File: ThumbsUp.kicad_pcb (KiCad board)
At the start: 2 copper layers, 215.3 x 223 mm, 51 parts, among them J1 52559-1233, J10 Raiser_Male, J13 Raiser_Female, J14 Raiser_Male, J19 Raiser_Female, J1L1 PJ-3200B, J1R1 PJ-3200B, J2 52559-1233, J33 Raiser_Male, J34 Raiser_Female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

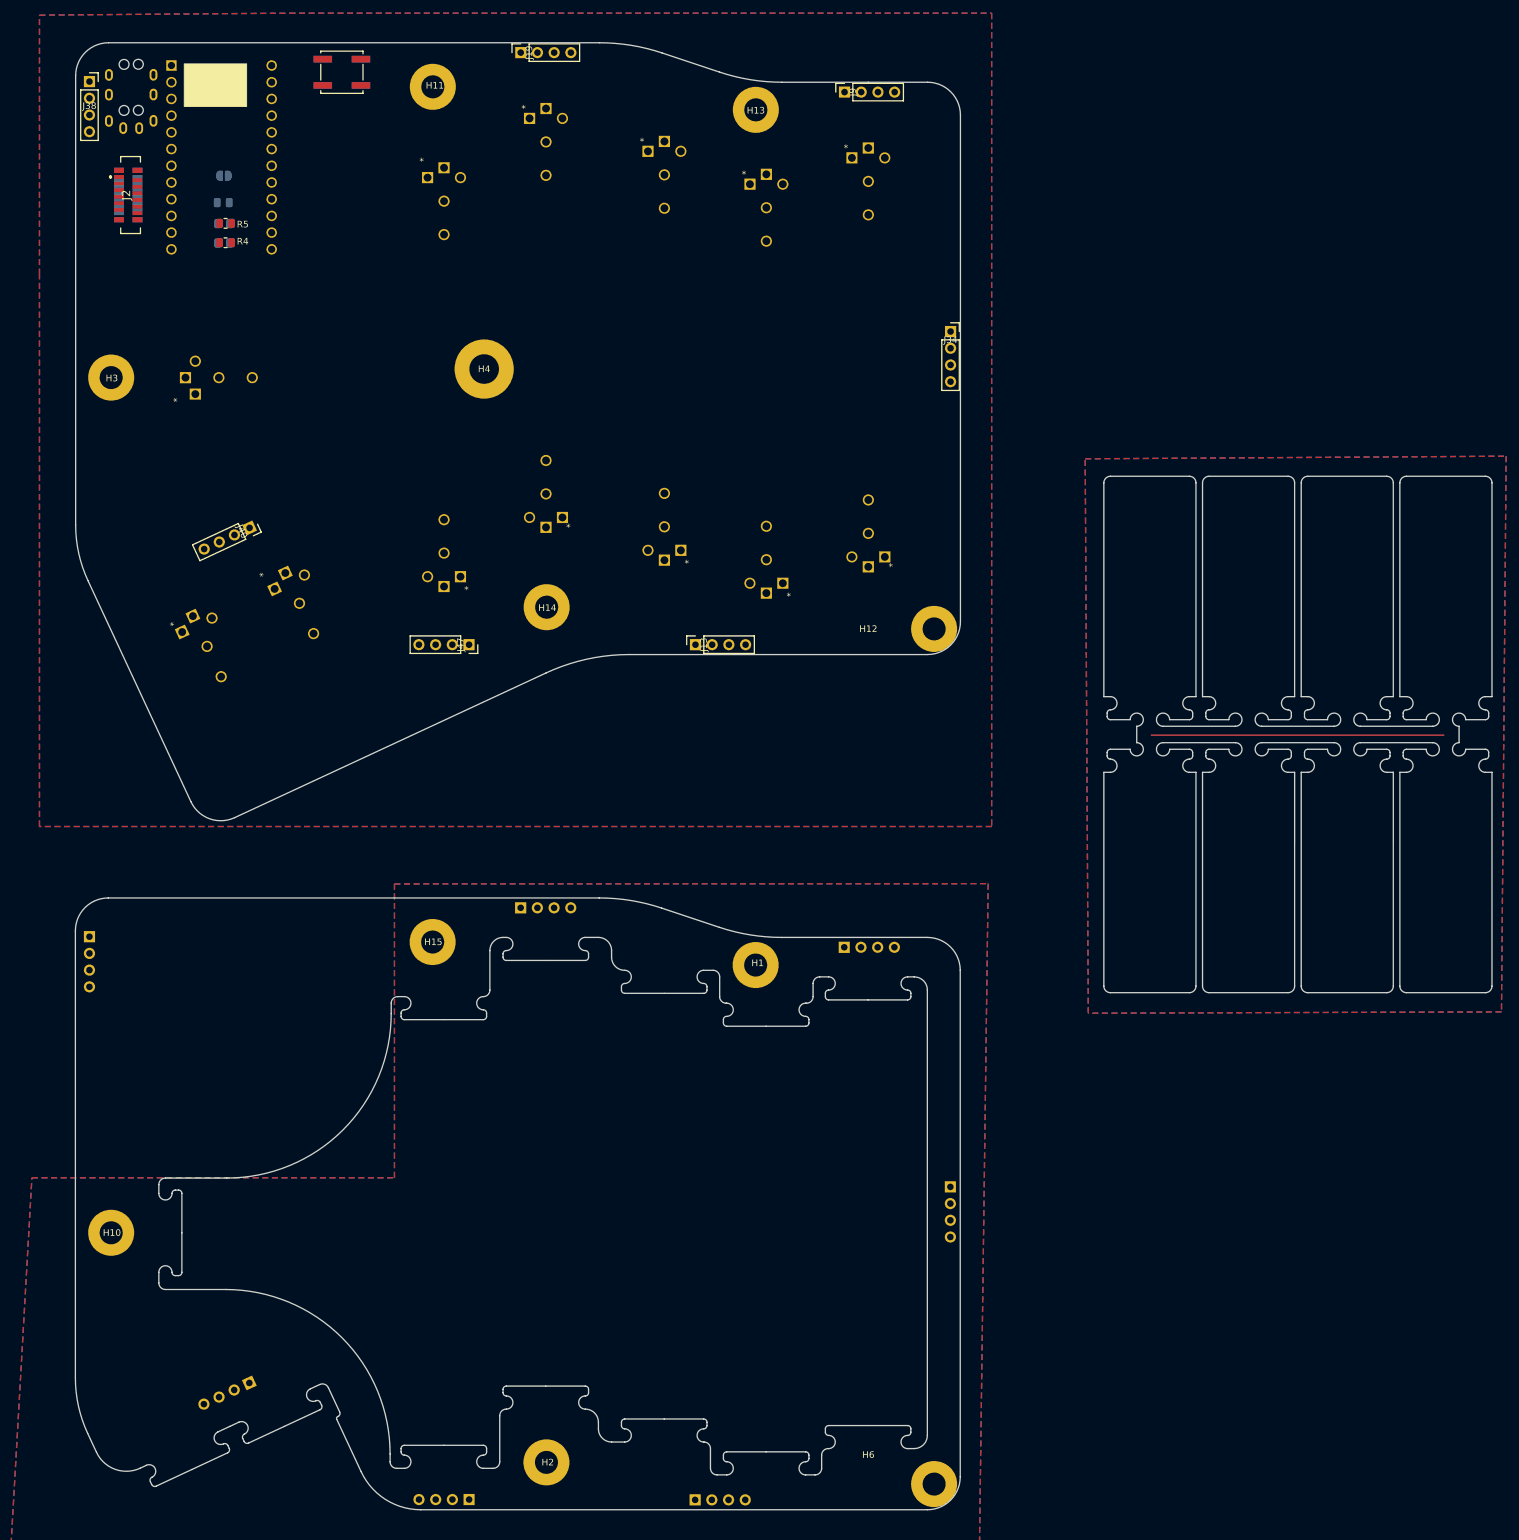
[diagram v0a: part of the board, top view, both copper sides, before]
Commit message: K12: Placed the tracks, text, etc. TODO: generate Gerbers.
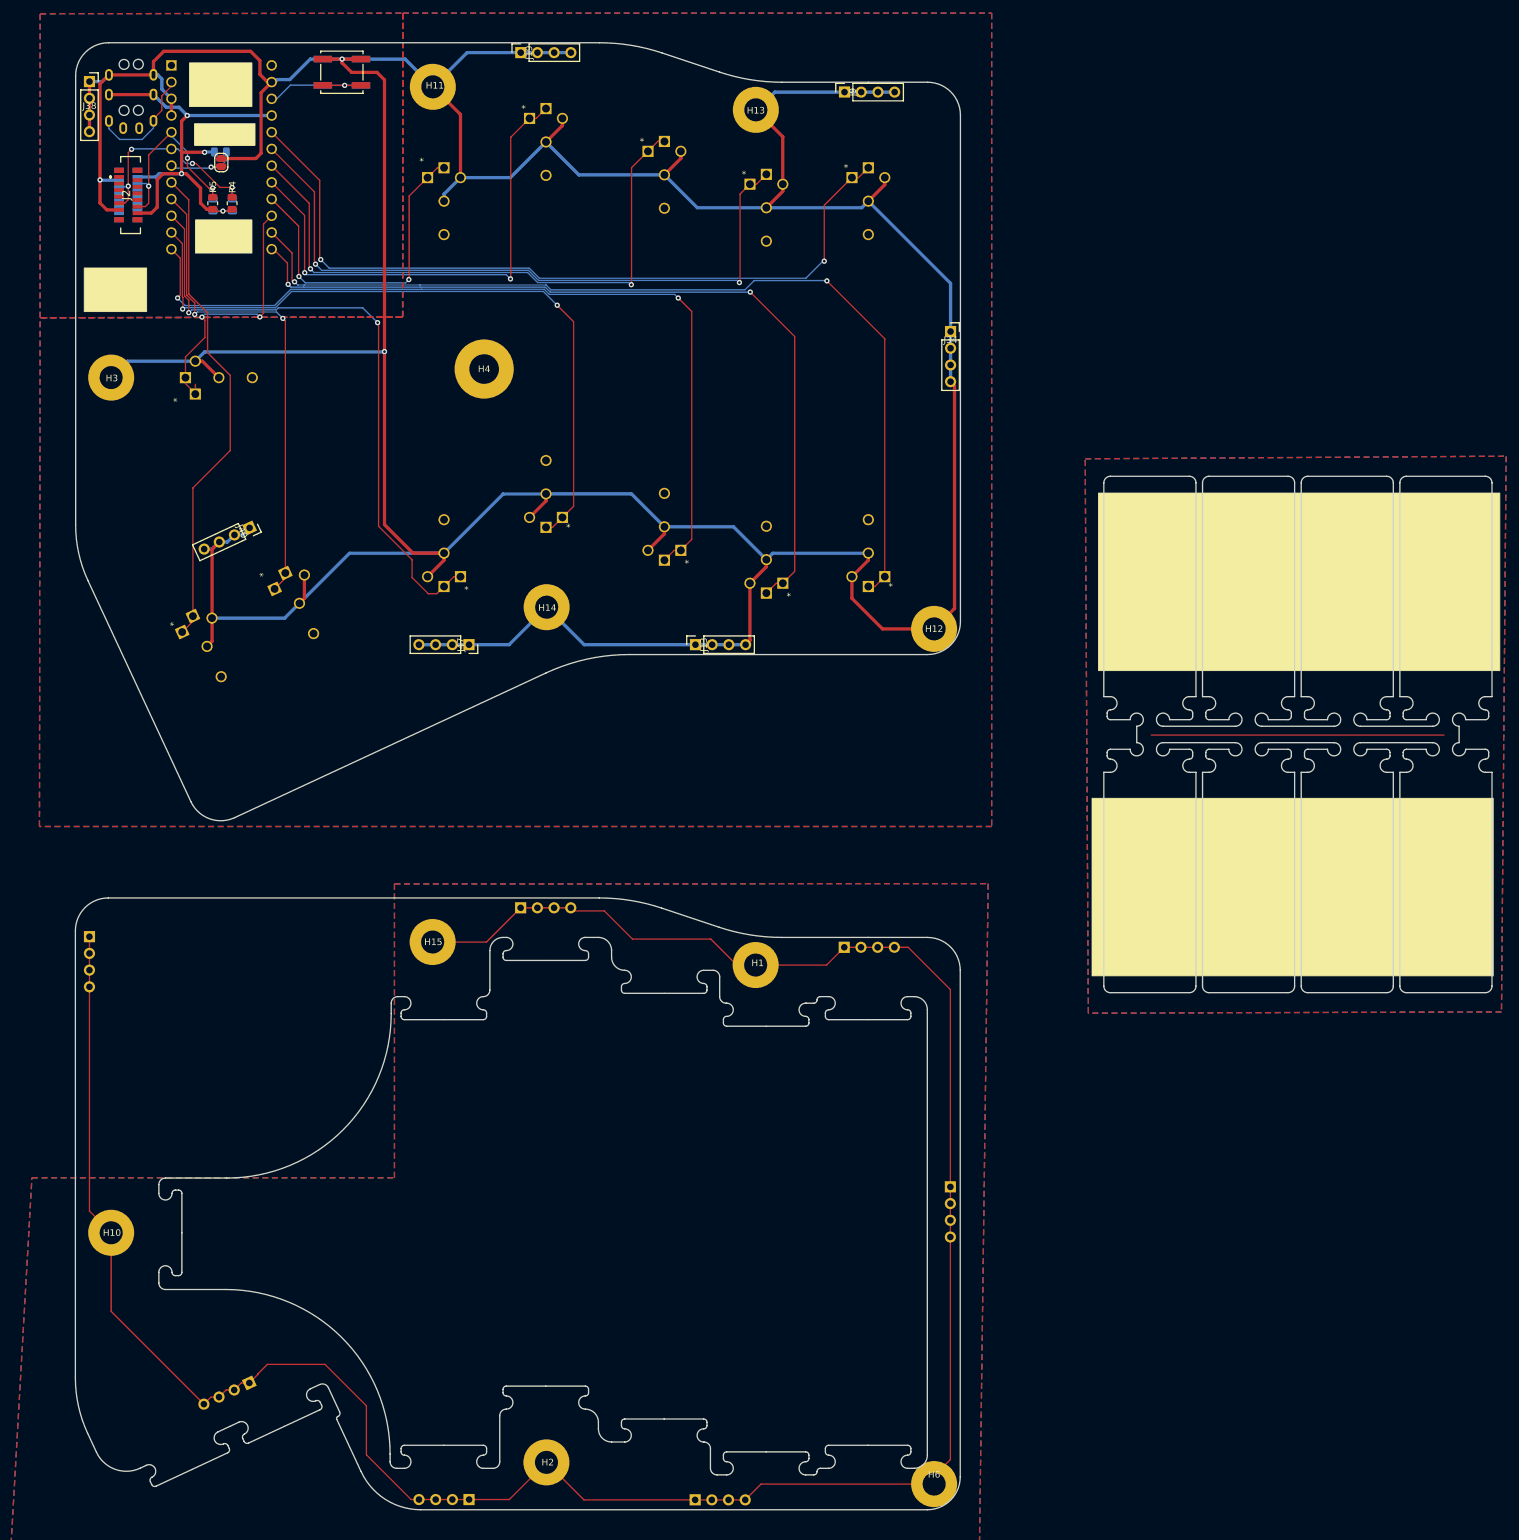
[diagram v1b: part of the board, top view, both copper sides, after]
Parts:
- JP1: moved to F.Cu
- moved H12 10.0 mm to (162.0, 114.6)
- moved H6 10.0 mm to (162.0, 244.6)
- moved R17 7.71 mm to (53.5, 42.1)
- moved R4 6.08 mm to (55.3, 49.9), turned to 90 degrees
- moved R2 5.93 mm to (55.3, 50.2), turned to 90 degrees
- moved R5 3.62 mm to (52.3, 49.9), turned to -90 degrees
- moved R1 3.26 mm to (52.4, 50.2), turned to -90 degrees
- moved MX42 3.00 mm to (152.0, 44.5)
- moved MX43 3.00 mm to (152.0, 108.2)
- moved JP1 2.04 mm to (53.6, 43.7), turned to -90 degrees
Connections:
- H4 pad 1: GND -> GND-B
- J1 pad 12: VCC -> L-RING1
- J2 pad 12: VCC -> L-RING1
- R1 pad 2: +3.3V -> L-RING1
- R2 pad 1: +3.3V -> L-RING1
- R4 pad 1: +3.3V -> L-RING1
- R5 pad 2: +3.3V -> L-RING1
- U1 pad 3: unconnected-(U1-GND-Pad3) -> GND
- U1 pad 4: unconnected-(U1-GND-Pad4) -> GND
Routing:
- net GND: track 0.00 -> 745.2 mm, vias 0 -> 3
- net GNDA: track 0.00 -> 374.8 mm
- net SwZ: track 0.00 -> 142.8 mm, vias 0 -> 2
- net SwG: track 0.00 -> 129.3 mm, vias 0 -> 2
- net SwS: track 0.00 -> 128.2 mm, vias 0 -> 2
- net SwD: track 0.00 -> 118.9 mm, vias 0 -> 2
- net SwB: track 0.00 -> 108.4 mm, vias 0 -> 2
- net SwT: track 0.00 -> 104.6 mm, vias 0 -> 2
- net SwR: track 0.00 -> 95.8 mm, vias 0 -> 2
- net SwL: track 0.00 -> 92.4 mm, vias 0 -> 2
- net SwP: track 0.00 -> 76.2 mm, vias 0 -> 2
- net SwE: track 0.00 -> 75.1 mm
- net SwU: track 0.00 -> 74.9 mm, vias 0 -> 2
- net L-RING1: track 0.00 -> 73.4 mm, vias 0 -> 4
- net SwF: track 0.00 -> 50.6 mm, vias 0 -> 2
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- added copper zone on B.Cu, net GND-B
- added copper zone on F.Cu, net GND-B
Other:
- outline, holes or cut-outs redrawn
- board text added: "5K FOR LEFT HAND"
- board text added: "LEFT HAND TRACKPAD PULLUP 5K"
- board text added: "RIGHT TRACKPAD PULLUP 5K"
- board text added: "u/ak66666 ThumbsUp! v.12 rev.3 March 2026"

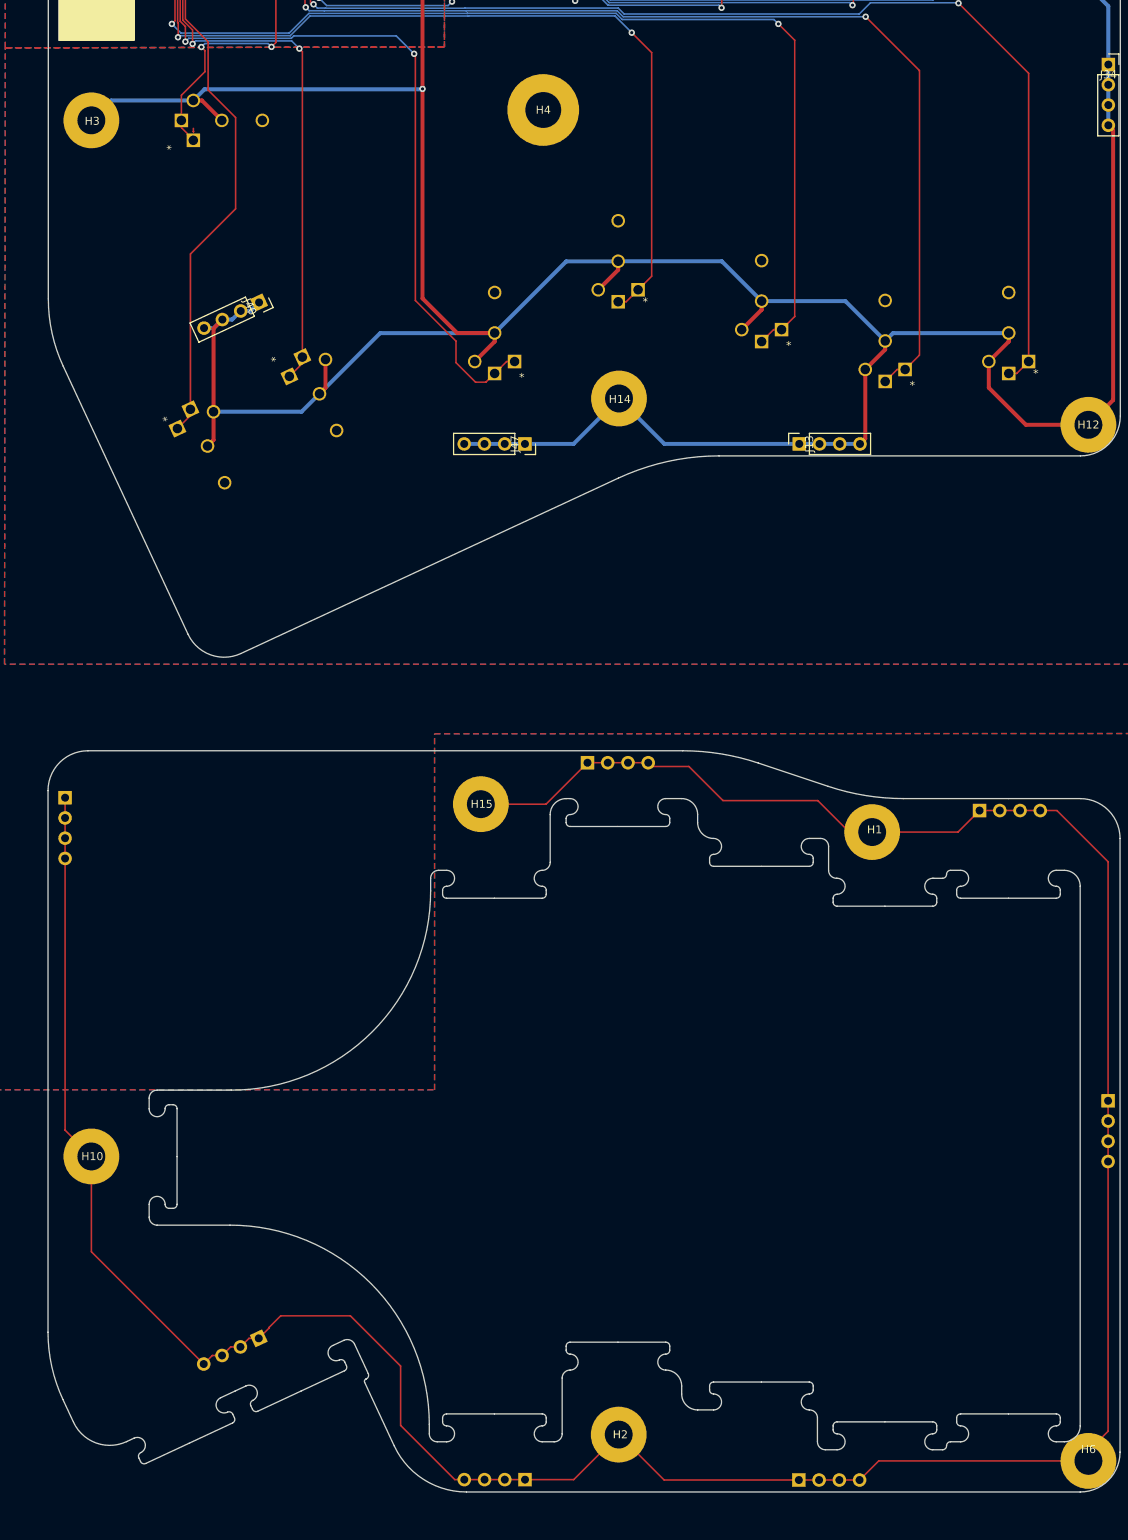
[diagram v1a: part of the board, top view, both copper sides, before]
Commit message: K12: Moved the thumb keys a bit up, closer to the fingers. TODO: generate Gerbers.
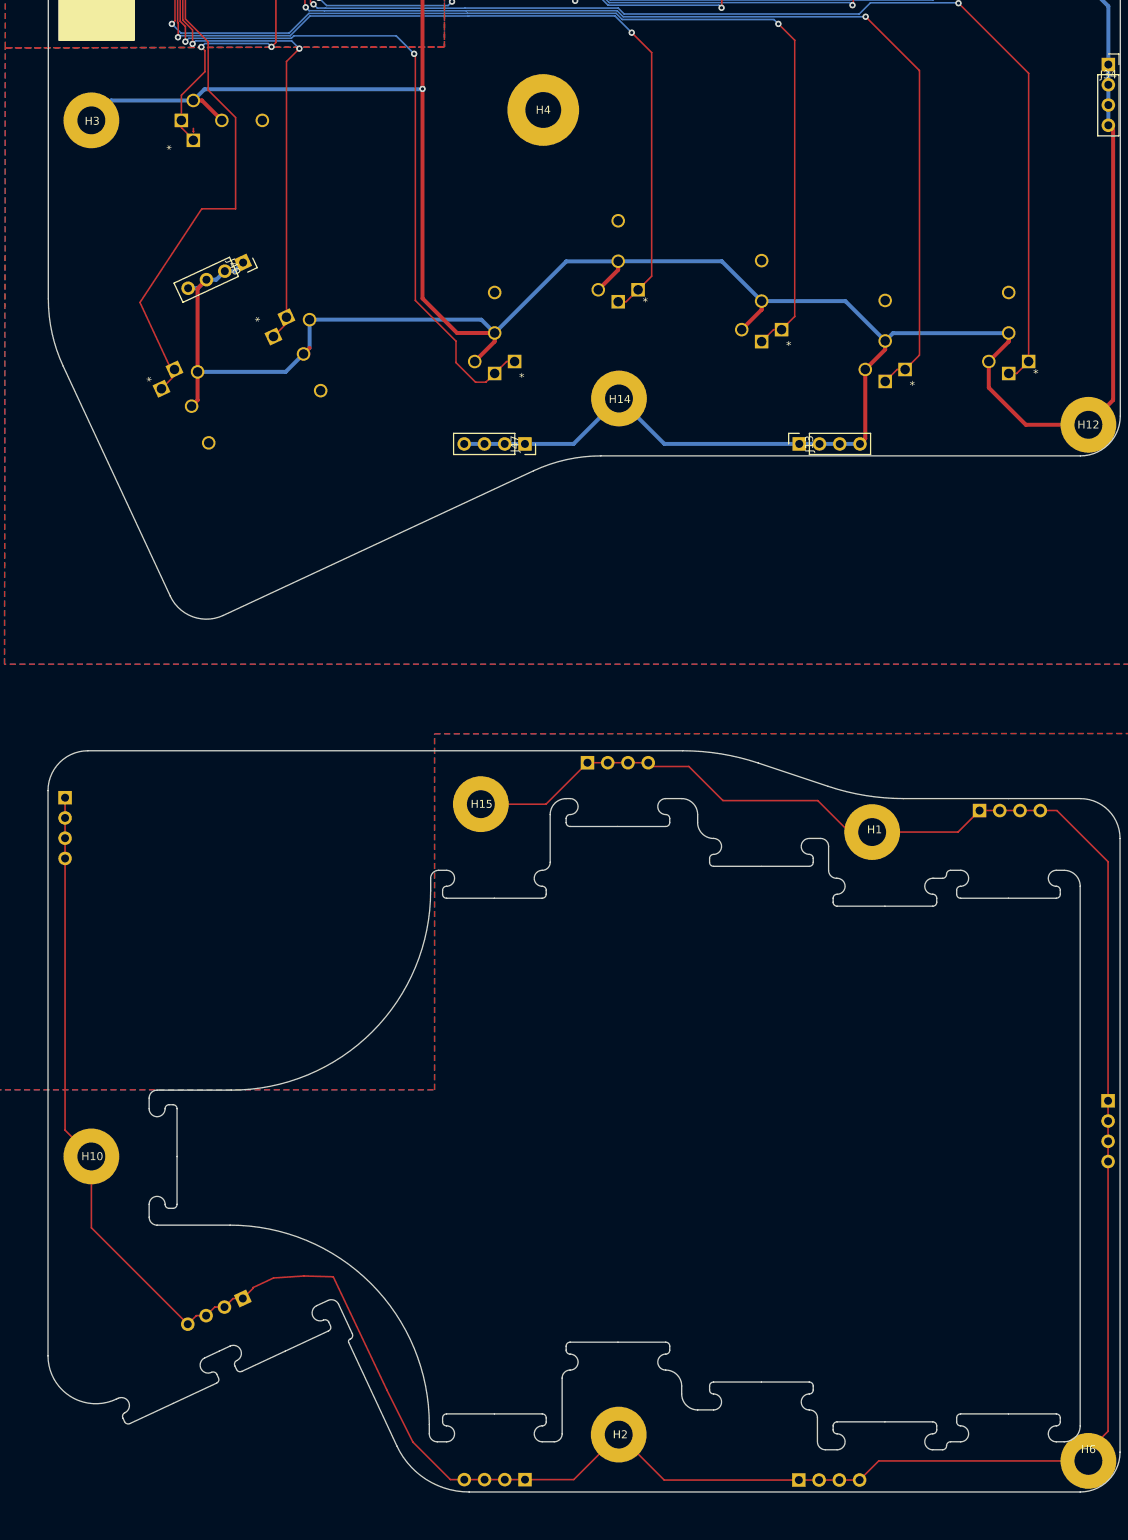
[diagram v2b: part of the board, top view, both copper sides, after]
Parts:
- moved J40 5.39 mm to (55.9, 94.2)
- moved J41 5.39 mm to (55.9, 224.2)
- moved MX26 5.39 mm to (61.4, 101.1)
- moved MX30 5.39 mm to (47.3, 107.7)
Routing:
- net SwU: track 74.9 -> 70.4 mm
- net GNDA: track 374.8 -> 372.8 mm
- net GND: track 745.2 -> 744.0 mm
- net SwE: track 75.1 -> 75.6 mm
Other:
- outline, holes or cut-outs redrawn

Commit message: K12: Moved the pinkie cluster 4mm out, 3mm down.//TODO: generate Gerbers
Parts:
- moved J10 8.08 mm to (155.8, 166.0)
- moved J9 8.08 mm to (155.9, 36.0)
- moved H1 3.91 mm to (137.4, 168.7)
- moved H12 3.91 mm to (164.5, 117.6)
- moved H13 3.91 mm to (137.4, 38.7)
- moved H6 3.91 mm to (164.5, 247.6)
- moved J13 3.91 mm to (128.2, 120.0)
- moved J34 3.91 mm to (167.0, 72.4)
- moved J35 3.91 mm to (167.0, 202.4)
- moved MX39 3.91 mm to (139.0, 48.5)
- moved MX40 3.91 mm to (139.0, 112.2)
- moved MX42 3.91 mm to (154.5, 47.5)
- moved MX43 3.91 mm to (154.5, 111.2)
- moved J14 3.91 mm to (128.2, 250.0)
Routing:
- net GND: track 744.0 -> 760.9 mm
- net GNDA: track 372.8 -> 384.5 mm
- net SwG: track 129.3 -> 125.2 mm
- net SwB: track 108.4 -> 104.4 mm
- net SwZ: track 142.8 -> 146.6 mm
- net SwS: track 128.2 -> 131.9 mm
- net SwD: track 118.9 -> 121.6 mm
- net SwT: track 104.6 -> 103.7 mm
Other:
- board size 215.3 x 223 mm -> 215.3 x 226 mm
